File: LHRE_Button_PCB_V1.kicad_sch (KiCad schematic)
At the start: 47 parts, among them J1 Conn_01x02, J2 Conn_01x02, J3 Conn_01x02, J4 Conn_01x08, J5 Conn_01x08, J6 Conn_01x12, J7 Conn_01x02, SW1 SW_DIP_x06, SW10 Dashboard_Button, SW11 Dashboard_Button, SW12 Dashboard_Button, SW2 SW_DIP_x06, SW3 SW_DIP_x06, SW4 Dashboard_Button, SW5 Dashboard_Button, SW6 Dashboard_Button, SW7 SW_DIP_x06, SW8 SW_DIP_x06, SW9 SW_DIP_x06

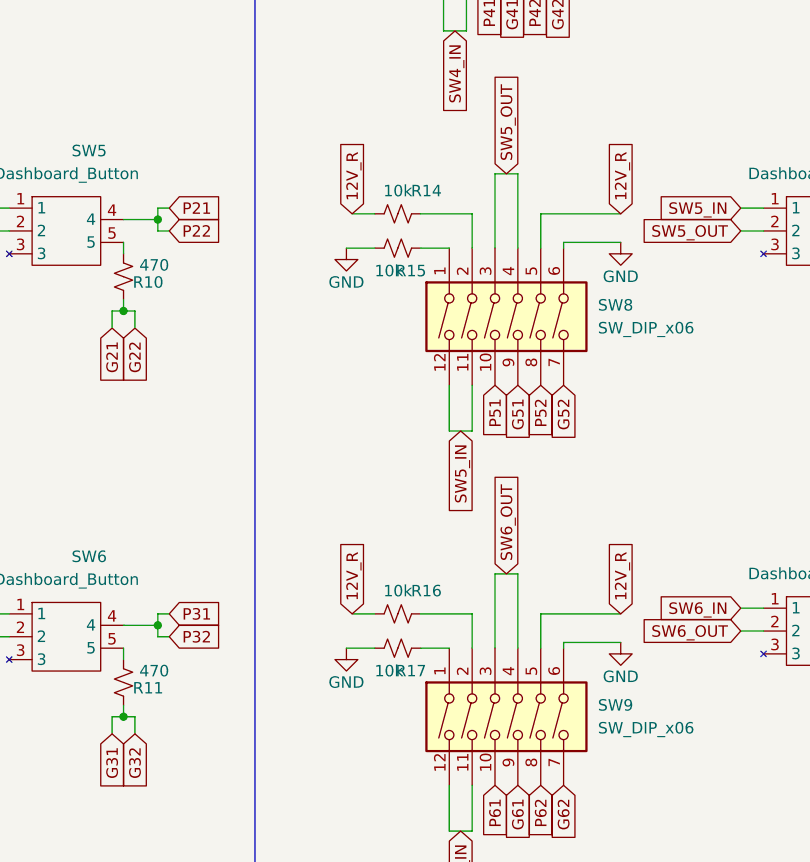
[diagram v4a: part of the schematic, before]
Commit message: changeed caps
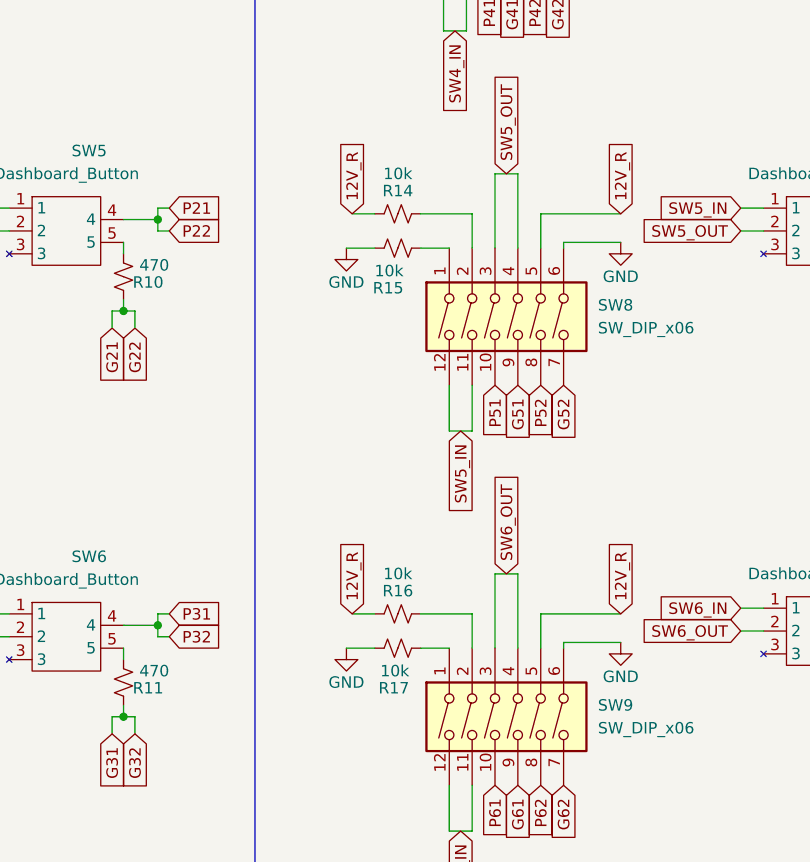
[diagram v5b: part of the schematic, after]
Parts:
- R1, R10, R11, R12, R13, R14, R15, R16, R17, R18, R19, R2, R20, R3, R4, R5, R6, R7, R8, R9: footprint Resistor_SMD:R_0603_1608Metric -> Resistor_SMD:R_0603_1608Metric_Pad0.98x0.95mm_HandSolder
